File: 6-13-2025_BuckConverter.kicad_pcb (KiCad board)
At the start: 2 copper layers, 45.5 x 28 mm, 17 parts, among them J1 6V to 35V, J2 5V 3A, U1 MP2338GTL-Z

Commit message: Completed PCB layout and routing.
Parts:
- moved J2 8.57 mm to (158.2, 75.8)
- moved R1 3.68 mm to (134.1, 59.8)
- moved R2 2.53 mm to (137.4, 62.2), turned to -90 degrees
- moved C5 1.79 mm to (141.5, 66.7)
- moved L1 1.67 mm to (147.2, 66.6)
- moved C4 1.51 mm to (148.6, 73.8)
- moved C3 1.51 mm to (148.6, 71.5)
- moved C6 1.34 mm to (135.3, 64.3)
- moved R5 1.34 mm to (132.9, 64.3)
- moved R4 1.34 mm to (130.9, 67.7), turned to 180 degrees
- moved C7 1.20 mm to (130.5, 64.3), turned to 90 degrees
- moved R6 1.13 mm to (128.2, 64.3), turned to 90 degrees
- moved R3 1.08 mm to (132.5, 69.9)
- moved J1 0.83 mm to (130.5, 77.9), turned to 180 degrees
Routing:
- net Net-(J2-VIN): track 0.00 -> 102.2 mm, vias 0 -> 4
- net Net-(J1-VIN): track 0.00 -> 20.9 mm, vias 0 -> 2
- net Net-(U1-EN): track 0.00 -> 10.1 mm
- net Net-(C7-Pad1): track 0.00 -> 7.34 mm
- net Net-(U1-FB): track 0.00 -> 5.49 mm
- net Net-(U1-SS): track 0.00 -> 4.26 mm
- net Net-(U1-PG): track 0.00 -> 4.21 mm
- net Net-(U1-BST): track 0.00 -> 3.64 mm
- net GND: vias 0 -> 28
- added copper zone on F.Cu, net GND
- added copper zone on F.Cu, net Net-(J1-VIN)
- added copper zone on F.Cu, net Net-(J2-VIN)
- added copper zone on F.Cu, net Net-(U1-SW)

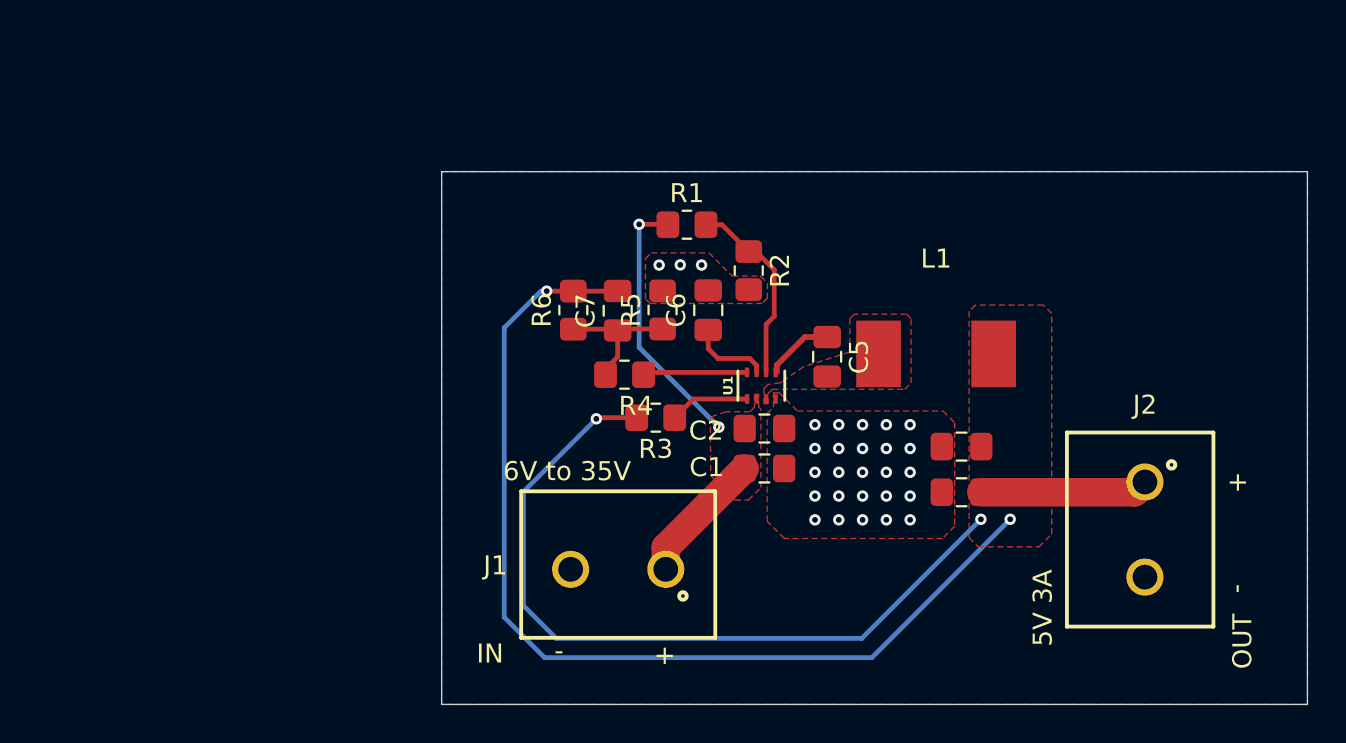
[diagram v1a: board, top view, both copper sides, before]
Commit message: Updated PCB layout, generated prototype gerber and drill files.
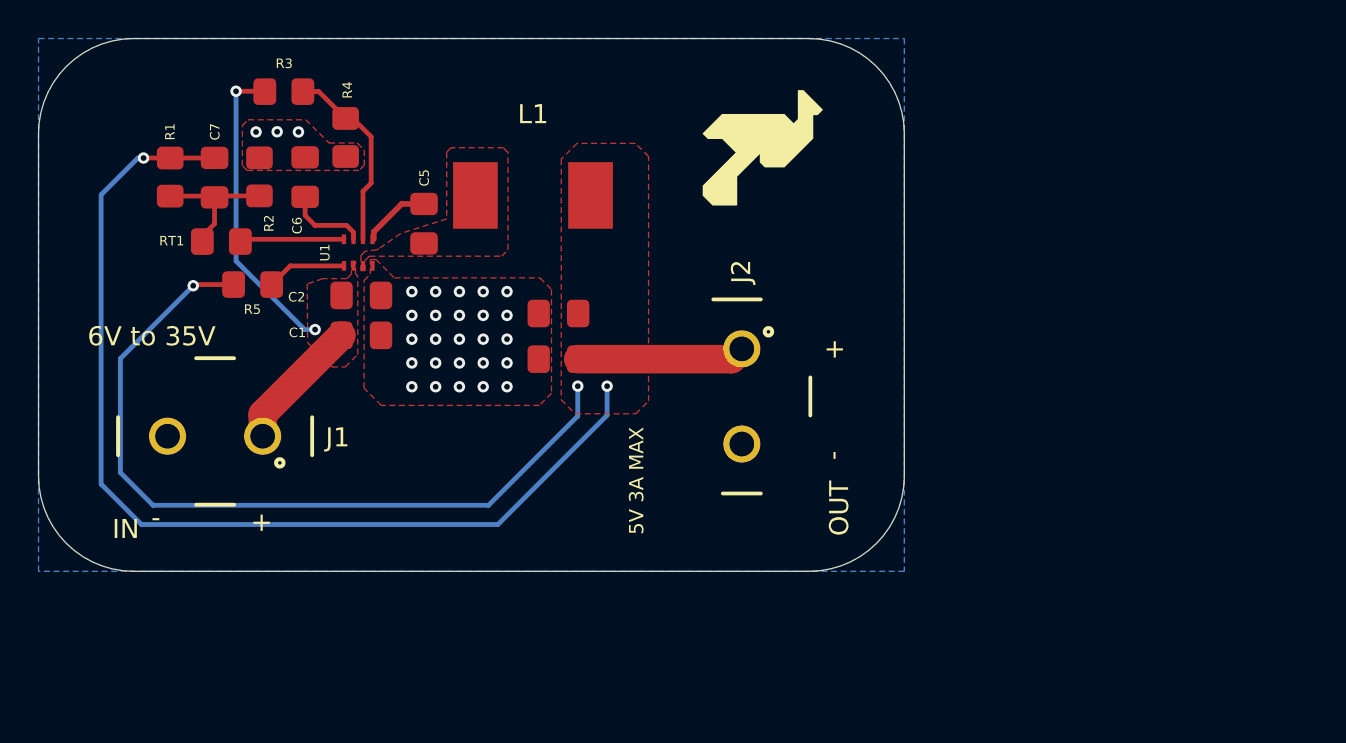
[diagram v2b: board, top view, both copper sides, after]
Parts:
- J1: footprint AlphaF:screw terminal -> AlphaF:TERM BLK 2POS SIDE ENTRY
- J2: value 5V 3A -> 5V 3A MAX; footprint AlphaF:screw terminal -> AlphaF:TERM BLK 2POS SIDE ENTRY
- L1: footprint AlphaF:inductor -> AlphaF:FIXED IND 6.8UH 4.5A
- moved L1 22.8 mm to (126.0, 58.2)
- moved R2 22.3 mm to (111.7, 57.3)
- moved RT1 22.3 mm to (109.7, 60.7)
- moved C7 22.3 mm to (109.3, 57.3)
- moved J1 22.3 mm to (109.3, 70.9)
- moved J2 22.3 mm to (137.0, 68.8)
- moved R5 22.3 mm to (111.3, 62.9)
- moved C1 22.3 mm to (117.0, 65.6)
- moved C2 22.3 mm to (117.0, 63.5)
- moved U1 22.3 mm to (116.9, 61.3)
- moved C3 22.3 mm to (127.4, 64.5)
- moved C5 22.3 mm to (120.3, 59.7)
- moved C6 22.3 mm to (114.1, 57.3)
- moved R1 22.3 mm to (107.0, 57.3)
- moved R3 22.3 mm to (113.0, 52.8)
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- renumbered R6 to R1, R5 to R2, R1 to R3, R2 to R4, R3 to R5, R4 to RT1
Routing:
- net Net-(J1-VIN): track 20.9 -> 23.1 mm
- net Net-(J2-VIN): track 102.2 -> 104.0 mm
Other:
- outline, holes or cut-outs redrawn

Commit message: Finalized layout and generated manufacturing files.
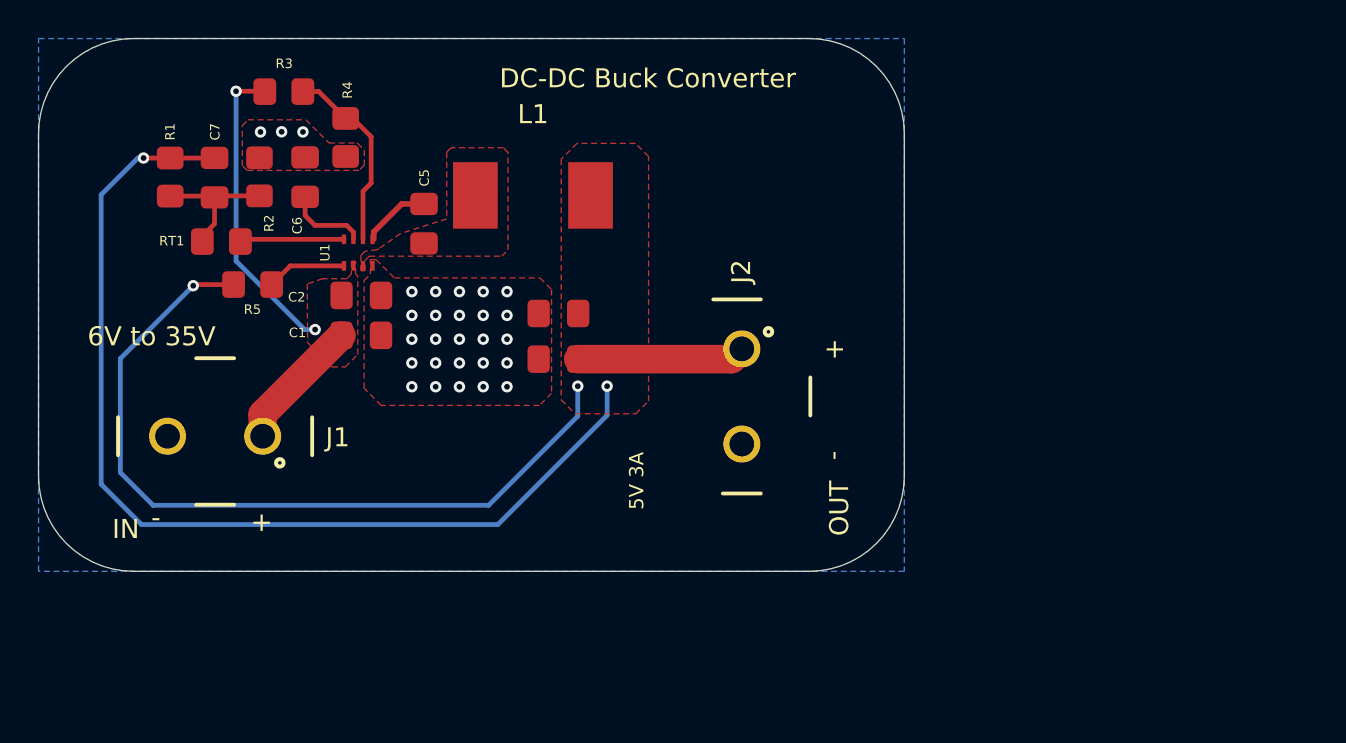
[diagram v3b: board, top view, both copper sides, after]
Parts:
- J2: value 5V 3A MAX -> 5V 3A
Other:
- board text added: "DC-DC Buck Converter"
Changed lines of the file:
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@@
 			(drillshape 0)
 			(scaleselection 1)
-			(outputdirectory "gerber/")
+			(outputdirectory "gerberFiles/")
 		)
 	)
@@
 			)
 		)
-		(property "Value" "5V 3A MAX"
+		(property "Value" "5V 3A"
 			(at 4.435 5.525 90)
 			(layer "F.SilkS")
@@
 		)
 	)
-	(gr_poly
-		(pts
-			(xy 140.75 54) (xy 140.75 55.25) (xy 139.25 56.75) (xy 138.25 56.75) (xy 138 56.5) (xy 138 56.25)
-			(xy 138 56) (xy 136.75 57.25) (xy 136.75 58.75) (xy 135.5 58.75) (xy 135 58.25) (xy 135 57.75) (xy 136.75 56)
-			(xy 136 55.25) (xy 135.25 55.25) (xy 135 55) (xy 136 54) (xy 139.25 54) (xy 139.75 54.5) (xy 140 54.25)
-			(xy 140 52.75) (xy 140.25 52.75) (xy 141.25 53.75) (xy 141 54)
-		)
-		(stroke
-			(width 0.0625)
-			(type solid)
-		)
-		(fill yes)
-		(layer "F.SilkS")
-	)
 	(gr_line
 		(start 145.565 55.005)
@@
 		)
 	)
+	(gr_text "DC-DC Buck Converter\n"
+		(at 124.29 52.69 0)
+		(layer "F.SilkS")
+		(effects
+			(font
+				(size 1 1)
+				(thickness 0.125)
+			)
+			(justify left bottom)
+		)
+	)
 	(gr_text "+"
 		(at 141.335 66.895 0)
@@
 	)
 	(via
-		(at 113.725 54.915)
+		(at 113.96 54.915)
 		(size 0.6)
 		(drill 0.3)
@@
 	)
 	(via
-		(at 112.605 54.905)
+		(at 112.84 54.905)
 		(size 0.6)
 		(drill 0.3)
@@
 	)
 	(via
-		(at 111.495 54.915)
+		(at 111.73 54.915)
 		(size 0.6)
 		(drill 0.3)
